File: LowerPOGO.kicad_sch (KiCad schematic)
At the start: 29 parts, among them J1 Conn_01x01_MountingPin, J10 Conn_01x01_MountingPin, J11 Conn_01x01_MountingPin, J12 Conn_01x01_MountingPin, J13 Conn_01x01_MountingPin, J14 Conn_01x01_MountingPin, J15 Conn_01x01_MountingPin, J16 Conn_01x01_MountingPin, J17 Conn_01x01_MountingPin, J18 Conn_01x01_MountingPin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

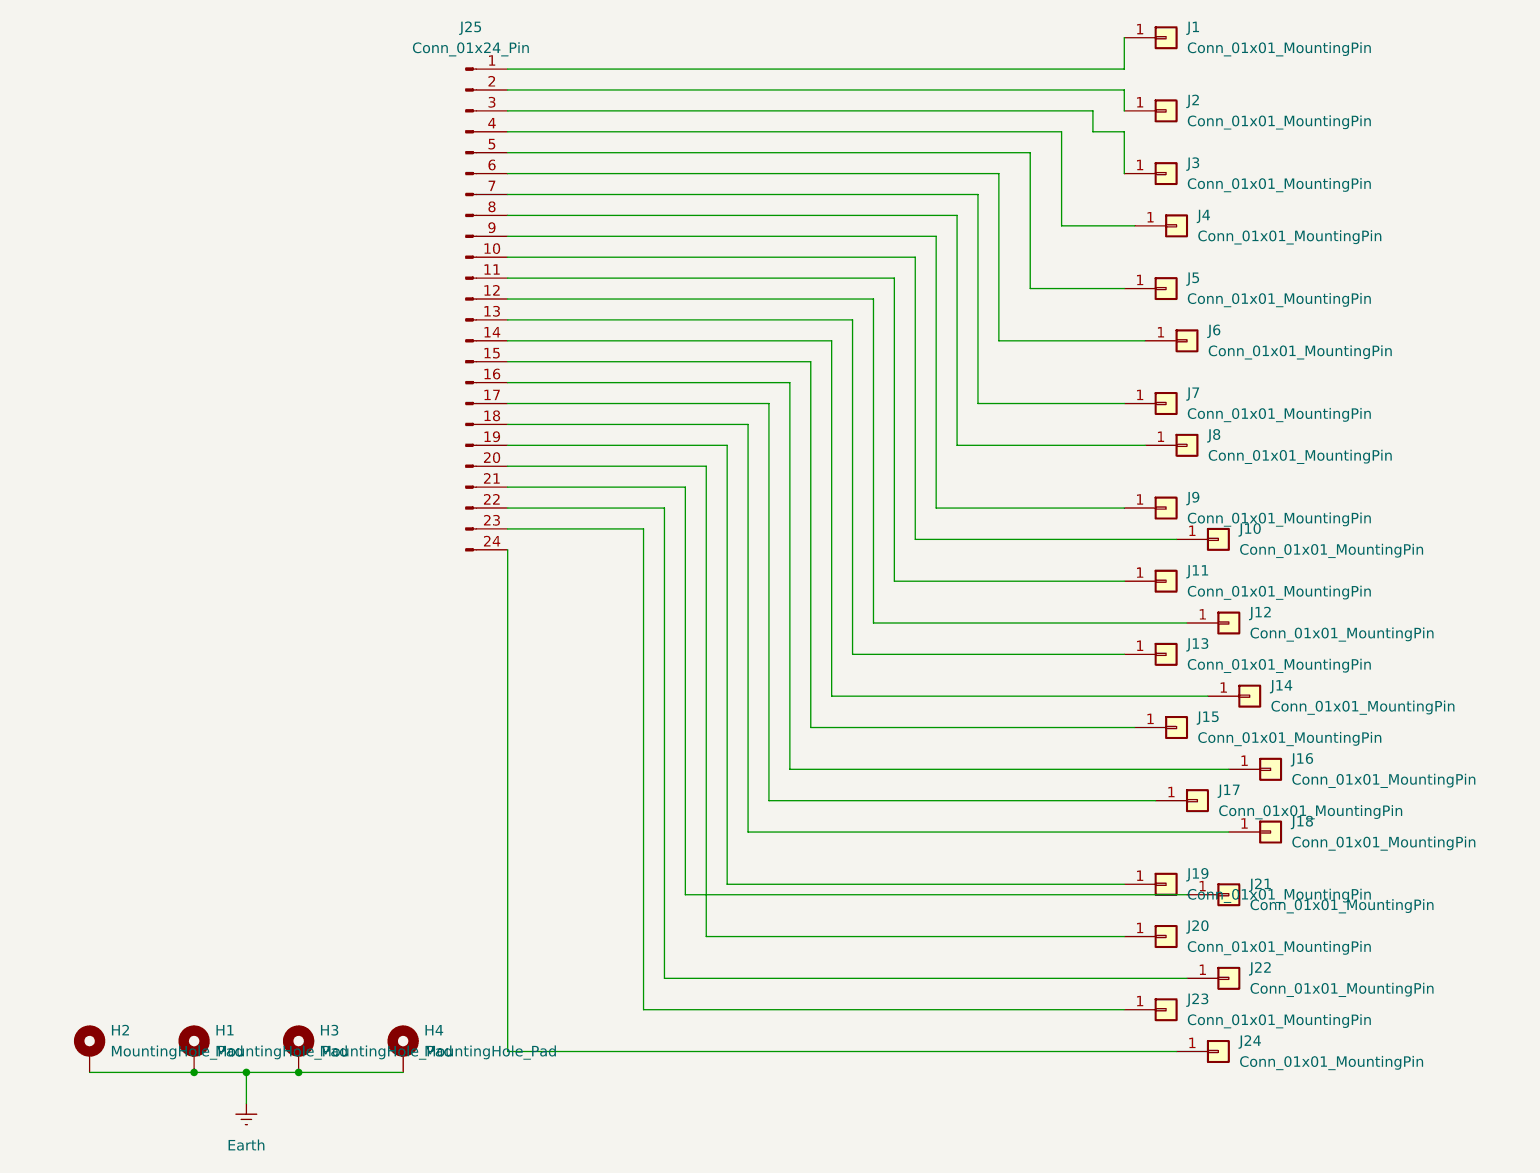
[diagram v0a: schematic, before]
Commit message: LowerPOGO v4 (2024-06-21) Resize J vias for proper fit inner diameter: 2.49mm outer diameter: 3.25mm
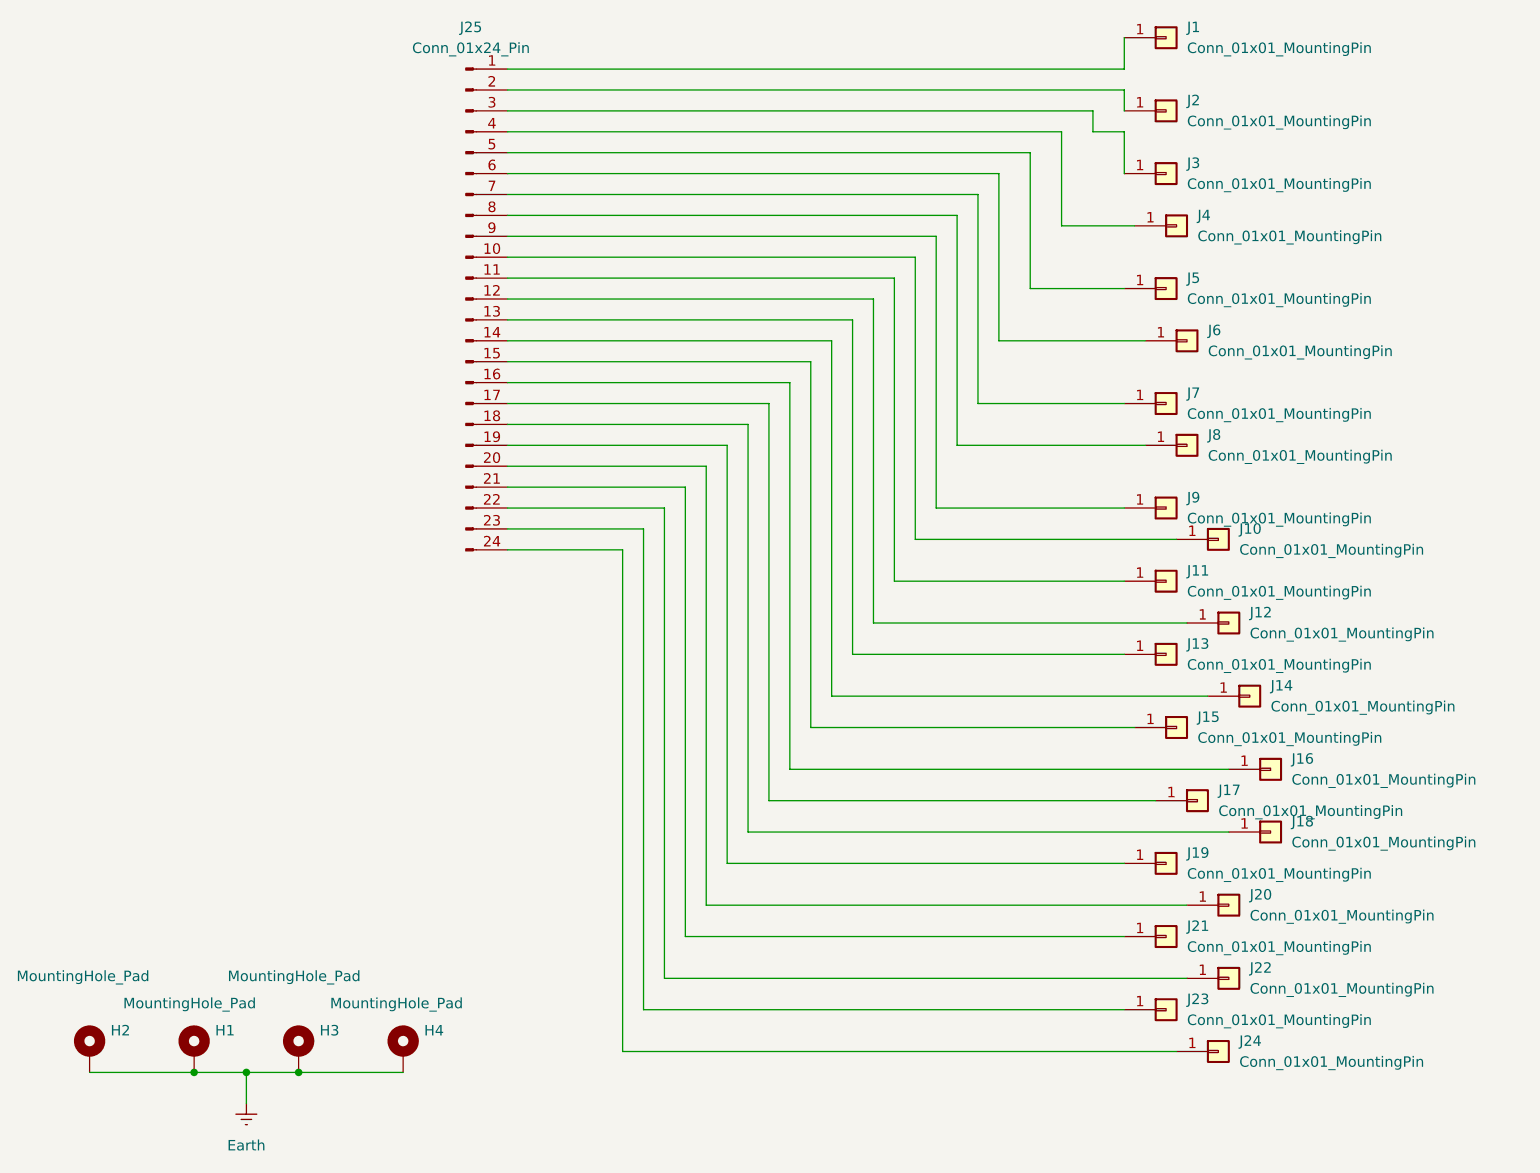
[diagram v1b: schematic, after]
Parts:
- J1, J10, J11, J12, J13, J14, J15, J16, J17, J18, J19, J2, J20, J21, J22, J23, J24, J3, J4, J5, J6, J7, J8, J9: footprint Connector_PinHeader_2.54mm:PinHeader_1x01_D2.54mm_Vertical -> Connector_PinHeader_2.54mm:PinHeader_1x01_D2.54mm_Vertical_PogoPin
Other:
- company: (none) -> QATCH Technologies LLC
- title: (none) -> Lower POGO Design
- moved on the sheet: J19, J20, J21

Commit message: Update KiCad designs for LowerPOGO to Multiport Design (v7) Tag fabrication outputs for this revision, remove Drawings.
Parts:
- removed J25: Conn_01x24_Pin, Connector_PinSocket_2.54mm:PinSocket_2x12_P2.54mm_Horizontal, symbol Connector:Conn_01x24_Pin
- added J25, J26, J27, J28, J29, J30: Conn_01x04_Pin, Connector_PinSocket_2.54mm:PinSocket_1x04_P2.54mm_Horizontal, symbol Connector:Conn_01x04_Pin
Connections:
- net at J24.1 (Pin_1): now also J30.4 (Pin_4)
- net at J23.1 (Pin_1): now also J30.3 (Pin_3)
- net at J12.1 (Pin_1): now also J27.4 (Pin_4)
- net at J8.1 (Pin_1): now also J26.4 (Pin_4)
- net at J11.1 (Pin_1): now also J27.3 (Pin_3)
- net at J1.1 (Pin_1): now also J25.1 (Pin_1)
- net at J10.1 (Pin_1): now also J27.2 (Pin_2)
- net at J13.1 (Pin_1): now also J28.1 (Pin_1)
- net at J14.1 (Pin_1): now also J28.2 (Pin_2)
- net at J15.1 (Pin_1): now also J28.3 (Pin_3)
- net at J16.1 (Pin_1): now also J28.4 (Pin_4)
- net at J17.1 (Pin_1): now also J29.1 (Pin_1)
- net at J18.1 (Pin_1): now also J29.2 (Pin_2)
- net at J19.1 (Pin_1): now also J29.3 (Pin_3)
- net at J2.1 (Pin_1): now also J25.2 (Pin_2)
- net at J20.1 (Pin_1): now also J29.4 (Pin_4)
- net at J21.1 (Pin_1): now also J30.1 (Pin_1)
- net at J22.1 (Pin_1): now also J30.2 (Pin_2)
- net at J3.1 (Pin_1): now also J25.3 (Pin_3)
- net at J4.1 (Pin_1): now also J25.4 (Pin_4)
- net at J5.1 (Pin_1): now also J26.1 (Pin_1)
- net at J6.1 (Pin_1): now also J26.2 (Pin_2)
- net at J7.1 (Pin_1): now also J26.3 (Pin_3)
- net at J9.1 (Pin_1): now also J27.1 (Pin_1)
